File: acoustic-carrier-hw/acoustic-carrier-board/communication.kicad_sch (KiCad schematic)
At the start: 48 parts, among them IC1 ECP5-BGA256, J9 HR911130A, U1 KSZ9031RN, Y1 25MHz

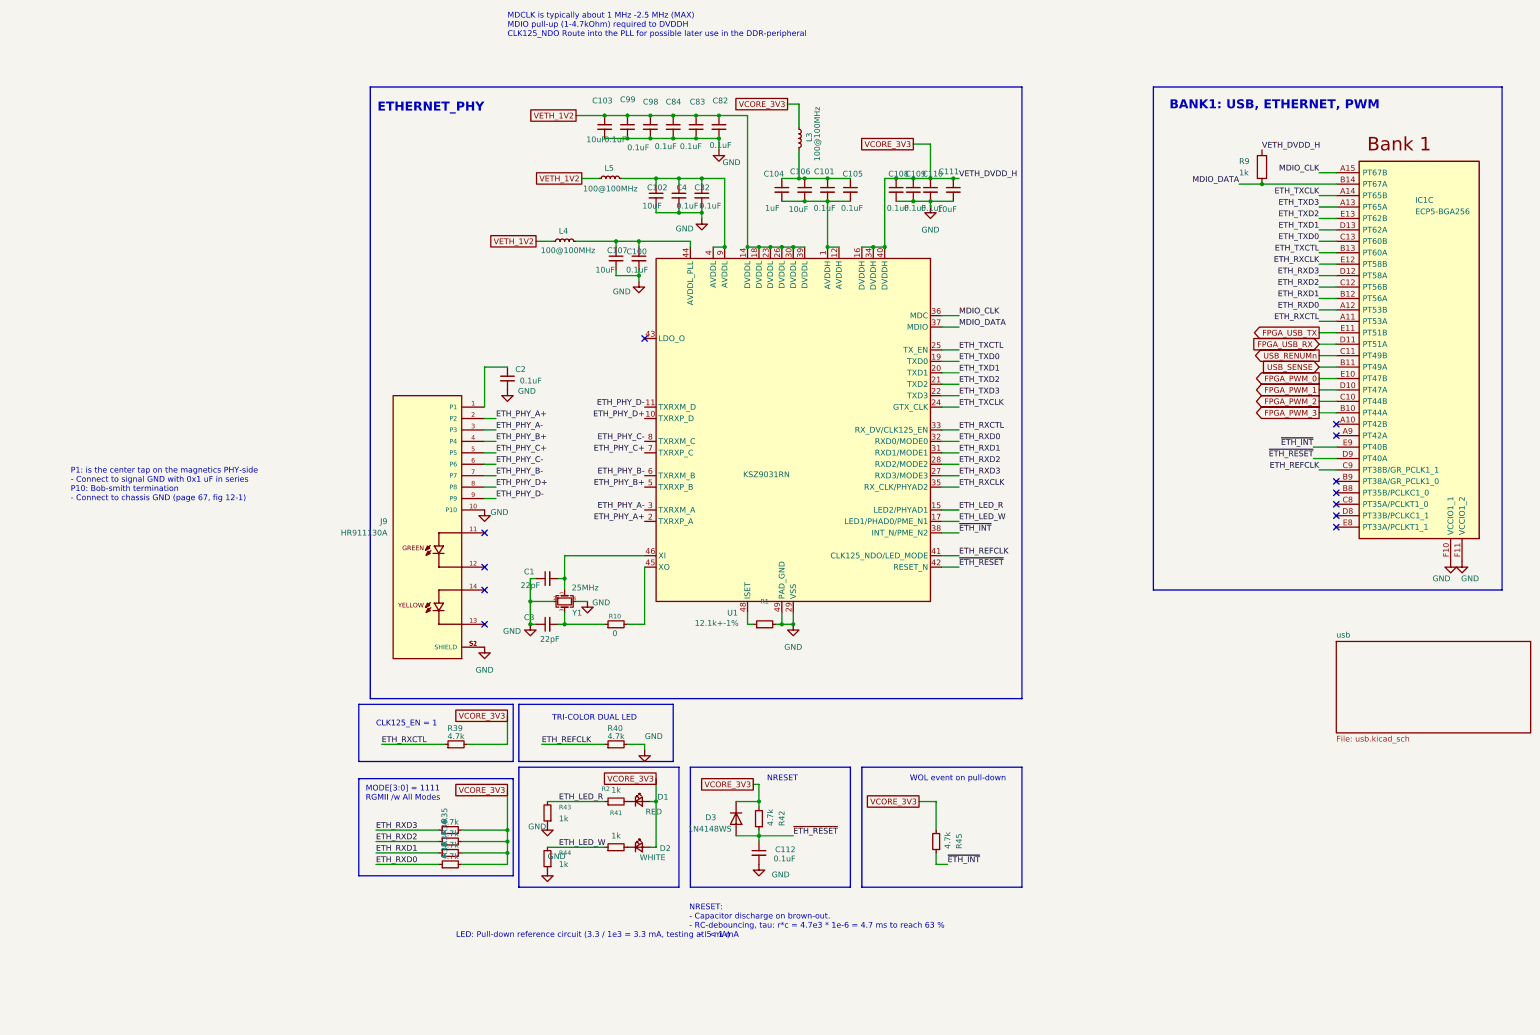
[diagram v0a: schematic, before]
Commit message: [carrier] removed external led, using ethernet leds, replaced 1kOhm by 470 ohm resistors
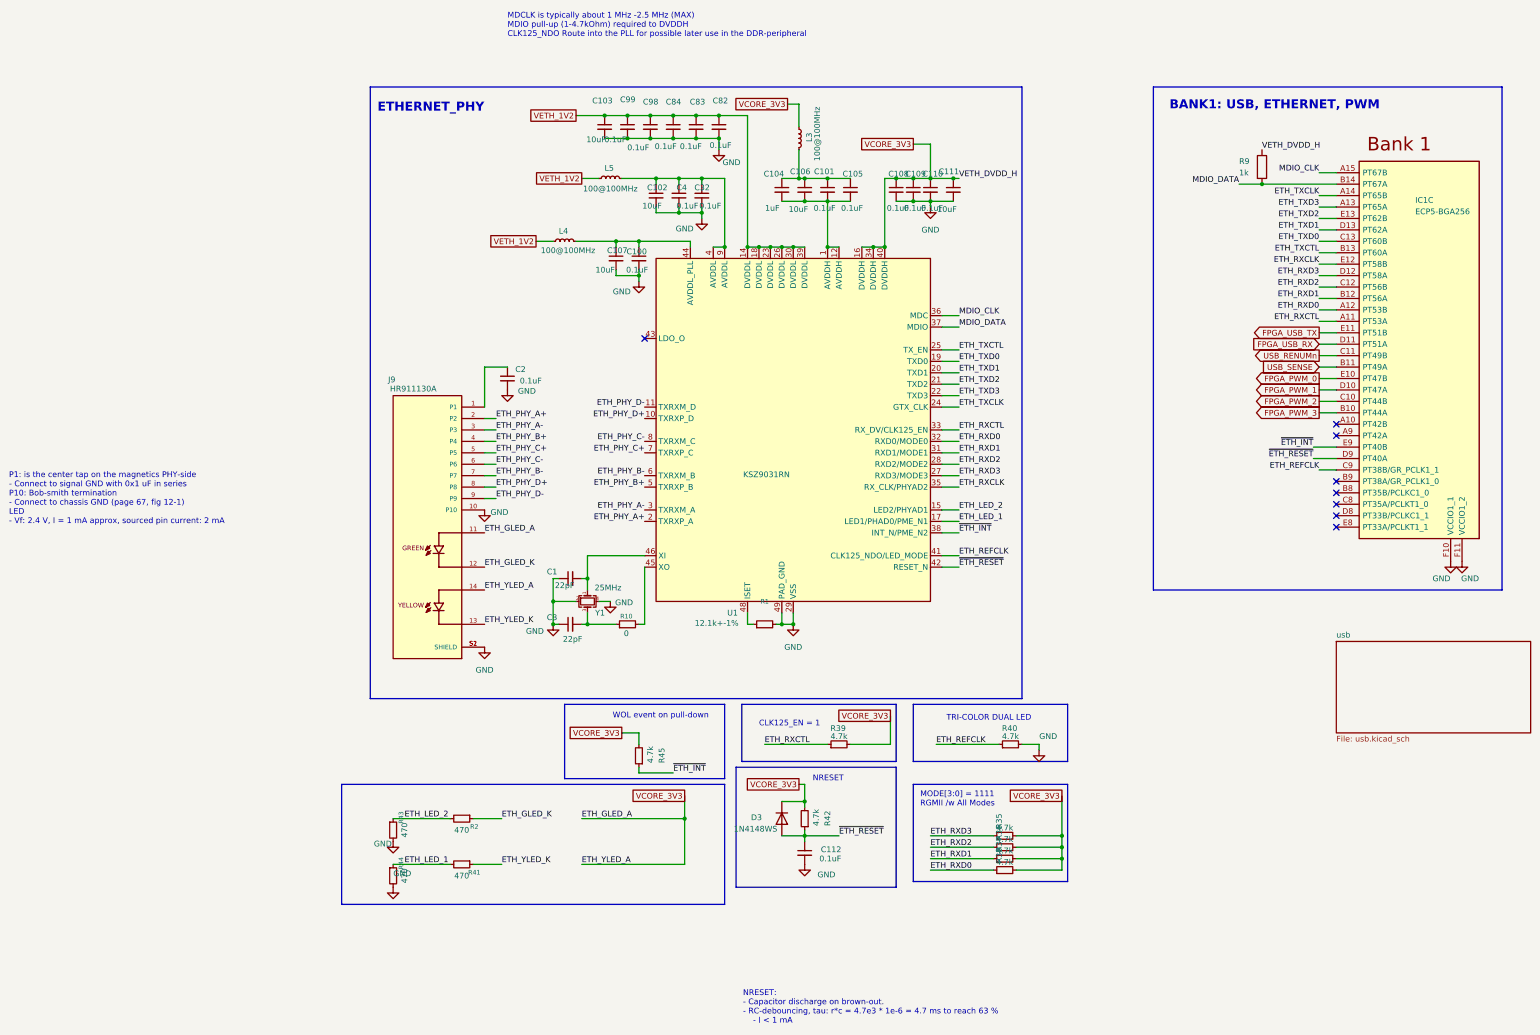
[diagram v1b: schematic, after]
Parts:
- removed D1: RED, Diode_SMD:D_0603_1608Metric, symbol Device:LED_Small
- removed D2: WHITE, Diode_SMD:D_0603_1608Metric, symbol Device:LED_Small
- R2, R41, R43, R44: value 1k -> 470; footprint Resistor_SMD:R_0402_1005Metric -> Resistor_SMD:R_0603_1608Metric; LPN C11702 -> C23179; MPN 0402WGF1001TCE -> 0603WAF4700T5E
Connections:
- net GND: now also R43.2, R44.2; no longer R43.1, R44.1
- net VCORE_3V3: now also J9.11, J9.14
- net ETH_LED_2: now reaches R2.2
- net ETH_LED_2: now also R43.1, U1.15 (LED2/PHYAD1)
- net ETH_GLED_K: now reaches J9.12
- net ETH_GLED_K: now also R2.1
- net ETH_YLED_K: now reaches J9.13
- net ETH_YLED_K: now also R41.1
- net ETH_LED_1: now reaches R41.2
- net ETH_LED_1: now also R44.1, U1.17 (LED1/PHAD0/PME_N1)
- removed net ETH_LED_R: R2.1, R43.2, U1.15 (LED2/PHYAD1)
- removed net ETH_LED_W: R41.1, R44.2, U1.17 (LED1/PHAD0/PME_N1)
- no-connect marks 12 -> 8
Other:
- note added: "P1: is the center tap on the magnetics PHY-side - Connect to signal GND with 0x1 uF in series P10: Bob-smith termination - Connect to chassis GND (page 67, fig 12-1) LED - Vf: 2.4 V, I = 1 mA approx, sourced pin current: 2 mA"
- note removed: "LED: Pull-down reference circuit (3.3 / 1e3 = 3.3 mA, testing at 5 mA)"
- note removed: "P1: is the center tap on the magnetics PHY-side - Connect to signal GND with 0x1 uF in series P10: Bob-smith termination - Connect to chassis GND (page 67, fig 12-1)"
- moved on the sheet: C1, C112, C3, D3, R10, R35, R36, R37, R38, R39, R40, R42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

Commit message: [carrier] Fixed most of the carrier board ERC issues (next) fix BGA ERC issue
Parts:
- IC1: footprint BGA256C80P16X16_1400X1400X170 -> fpga:BGA256C80P16X16_1400X1400X170; LPN (none) -> C1521614; MPN (none) -> LFE5U-25F-6BG256C; Part Number LFE5U-12F-6BG256C -> LFE5U-25F-6BG256C
- J9: Availability (none) -> In Stock; Check_prices (none) -> https://www.snapeda.com/parts/HR911130A/HanRun/view-part/?r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; MANUFACTURER (none) -> HanRun; MAXIMUM_PACKAGE_HEIGHT (none) -> 13.75 mm; MF (none) -> hanrun; MP (none) -> HR911130A; PARTREV (none) -> A; Package (none) -> None; Price (none) -> None; STANDARD (none) -> Manufacturer Recommendations; SnapEDA_Link (none) -> https://www.snapeda.com/parts/HR911130A/HanRun/view-part/?r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
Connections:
- net at C101.1, C104.1, C105.1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: now also U1.1 (AVDDH), U1.12 (AVDDH)
- net at C101.2, C104.2, C105.2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: no longer U1.1 (AVDDH), U1.12 (AVDDH)
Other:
- moved on the sheet: C112, D3, R2, R41, R42, R43, R44

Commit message: [carrier] Fixed ERC errors and fpga-footprints (next) ) add extra pin functionality to 2 remaining banks, perform schematic checks
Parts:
- IC1: Part Number LFE5U-25F-6BG256C -> (none)
